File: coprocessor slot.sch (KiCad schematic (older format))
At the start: 17 parts, among them CN600 CO-PROCESSOR_SLOT, U600 74LS245, U601 74LS245, U602 74ALS245, U603 74LS245, U604 74LS245, U605 74ALS245

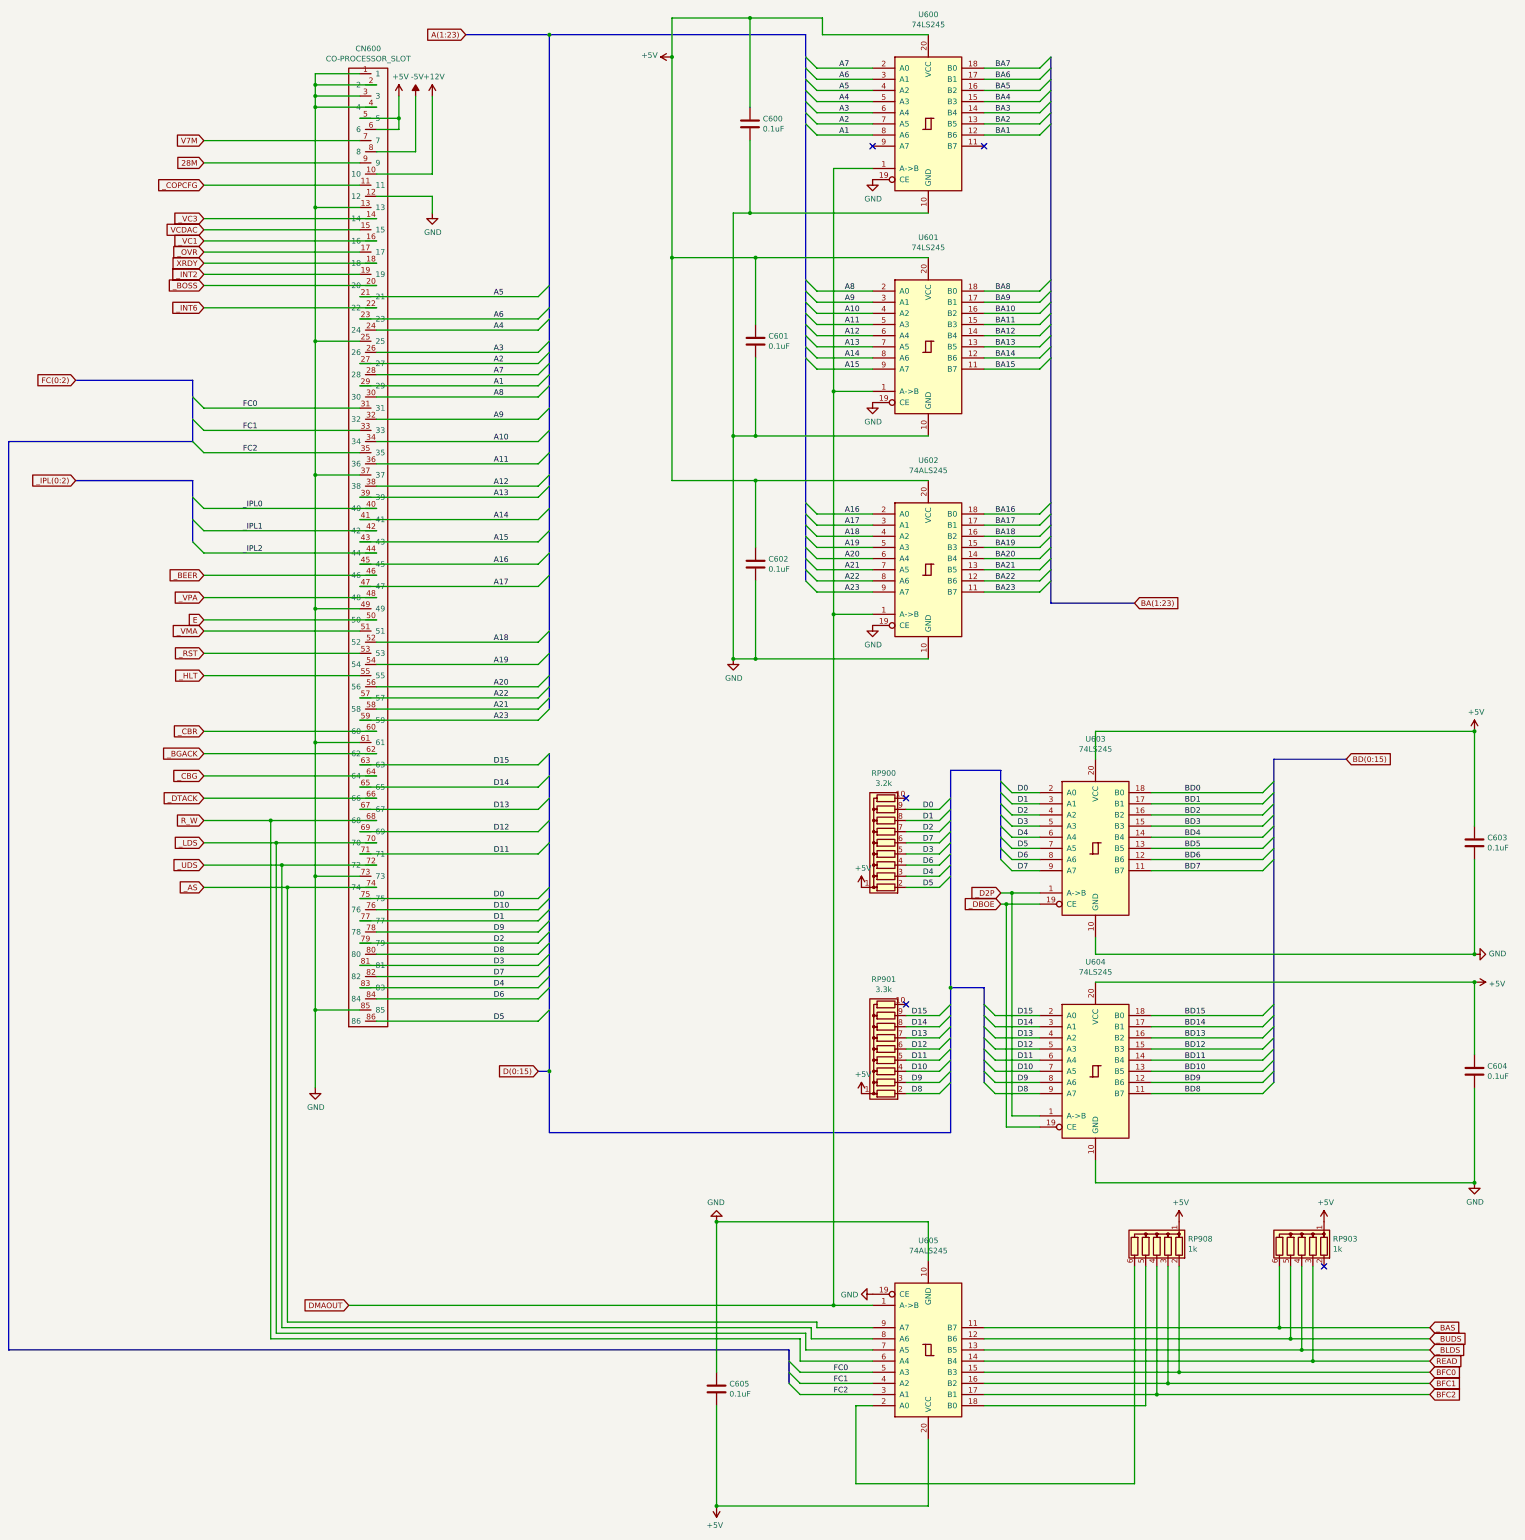
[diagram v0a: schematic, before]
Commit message: Rename bus with correct syntax
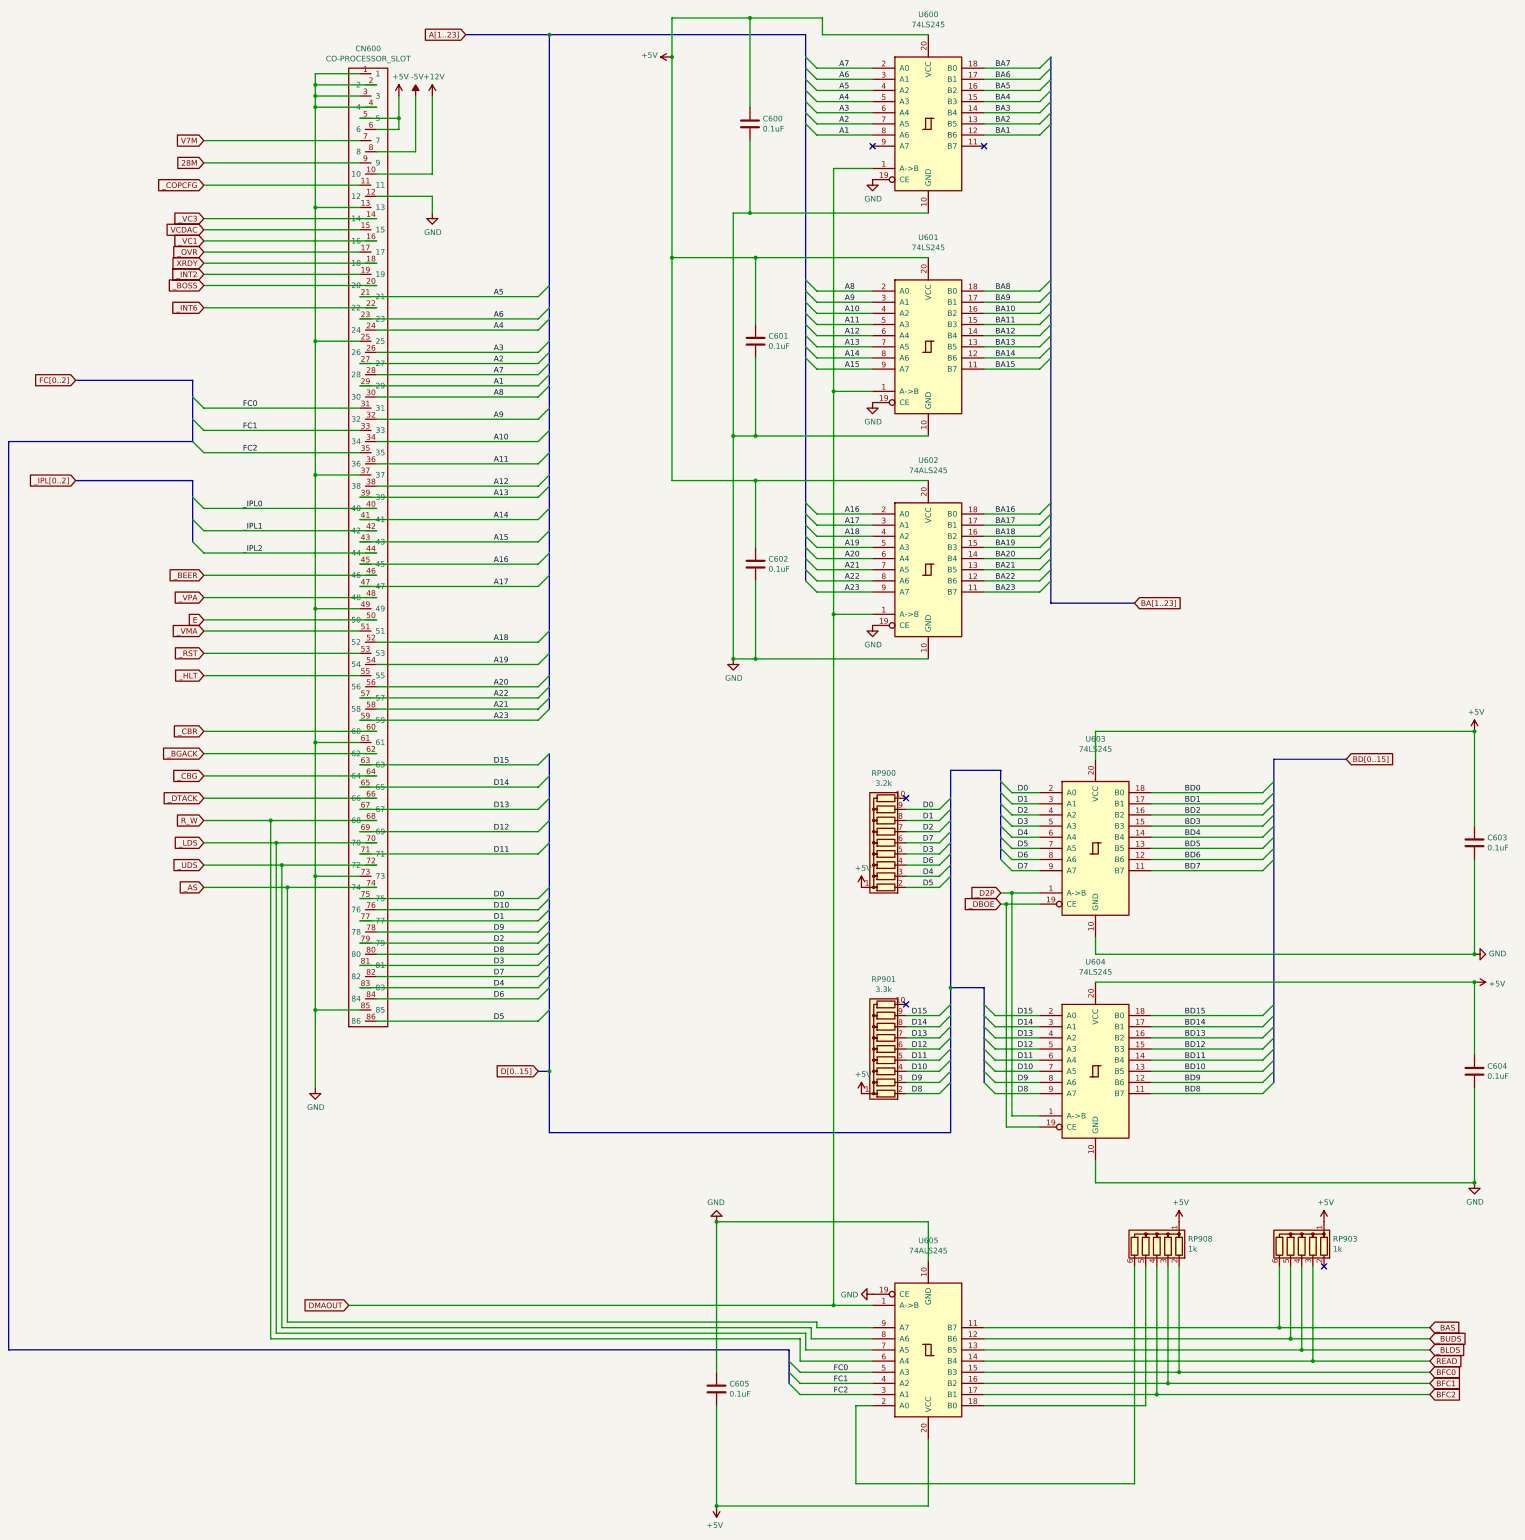
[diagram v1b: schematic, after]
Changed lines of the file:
@@
-EESchema Schematic File Version 4
+EESchema Schematic File Version 5
 LIBS:amiga2000-cache
 EELAYER 29 0
@@
 	4400 3800 3350 3800
 Text GLabel 3350 3800 0    50   Input ~ 0
-FC(0:2)
+FC[0..2]
 Wire Wire Line
 	6050 4950 4500 4950
@@
 _IPL2
 Text GLabel 3350 4700 0    50   Input ~ 0
-_IPL(0:2)
+_IPL[0..2]
 Wire Wire Line
 	6050 6950 4500 6950
@@
 	6850 700  7600 700
 Text GLabel 6850 700  0    50   Input ~ 0
-A(1:23)
+A[1..23]
 Wire Wire Line
 	5900 7250 7500 7250
@@
 	7600 10000 7500 10000
 Text GLabel 7500 10000 0    50   Input ~ 0
-D(0:15)
+D[0..15]
 $Comp
 L 74xx:74LS245 U600
@@
 	14100 7200 14750 7200
 Text GLabel 14750 7200 2    50   Input ~ 0
-BD(0:15)
+BD[0..15]
 Wire Bus Line
 	12100 5800 12850 5800
 Text GLabel 12850 5800 2    50   Input ~ 0
-BA(1:23)
+BA[1..23]
 $Comp
 L power:+5V #PWR0245
@@
 Wire Wire Line
 	11000 13900 11000 13300
-Wire Bus Line
-	4400 3800 4400 4350
-Wire Bus Line
-	4400 4700 4400 5250
-Wire Bus Line
-	9750 12500 9750 12800
-Wire Bus Line
-	11650 7300 11650 8100
-Wire Bus Line
-	11500 9250 11500 10100
-Wire Bus Line
-	11200 7300 11200 9250
-Wire Bus Line
-	11200 9250 11200 10550
-Wire Bus Line
-	7600 700  7600 6750
-Wire Bus Line
-	7600 7150 7600 10000
-Wire Bus Line
-	9900 700  9900 5600
-Wire Bus Line
-	14100 7200 14100 10100
-Wire Bus Line
-	12100 900  12100 5800
 $Comp
 L power:GND #PWR0241
@@
 $EndComp
 Connection ~ 9100 13900
+Wire Bus Line
+	4400 3800 4400 4350
+Wire Bus Line
+	4400 4700 4400 5250
+Wire Bus Line
+	9750 12500 9750 12800
+Wire Bus Line
+	11650 7300 11650 8100
+Wire Bus Line
+	11500 9250 11500 10100
+Wire Bus Line
+	11200 7300 11200 9250
+Wire Bus Line
+	11200 9250 11200 10550
+Wire Bus Line
+	7600 700  7600 6750
+Wire Bus Line
+	7600 7150 7600 10000
+Wire Bus Line
+	9900 700  9900 5600
+Wire Bus Line
+	14100 7200 14100 10100
+Wire Bus Line
+	12100 900  12100 5800
 $EndSCHEMATC

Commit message: REV 6.2 fixes applied
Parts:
- RP900: value 3.2k -> 3.3k
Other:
- note added: "REV 6.2 fixes: RP900 and RP901, 3.3k both, connected to D[0..15] were removed\nAnd instead connected directly to U603 and U604\nHere they get the same name"

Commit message: Fix the fixes
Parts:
- renumbered RP900 to RPF603, RP901 to RPF604
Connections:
- net +5V: no longer RPF603.1 (common), RPF604.1 (common)
- net D3: now also RPF603.6 (R5); no longer RPF603.5 (R4)
- net D4: now also RPF603.5 (R4); no longer RPF603.3 (R2)
- net D5: now also RPF603.4 (R3); no longer RPF603.2 (R1)
- net D6: now also RPF603.3 (R2); no longer RPF603.4 (R3)
- net D7: now also RPF603.2 (R1); no longer RPF603.6 (R5)
- net GND: now also RPF603.1 (common), RPF604.1 (common)
- net _D2P: now also RPF603.10 (R9), RPF604.10 (R9)
- no-connect marks 5 -> 3
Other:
- note added: "REV 6.2 fixes: RP900 and RP901, 3.3k both, connected to D[0..15] were removed\nAnd instead connected directly to U603 and U604"
- note removed: "REV 6.2 fixes: RP900 and RP901, 3.3k both, connected to D[0..15] were removed\nAnd instead connected directly to U603 and U604\nHere they get the same name"
- moved on the sheet: RPF603
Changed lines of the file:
@@
 $EndComp
 Connection ~ 9100 13900
+Text Notes 8450 7100 0    50   ~ 0
+REV 6.2 fixes: RP900 and RP901, 3.3k both, connected to D[0..15] were removed\nAnd instead connected directly to U603 and U604
+Entry Wire Line
+	11100 10100 11200 10000
+Entry Wire Line
+	11100 10000 11200 9900
+Entry Wire Line
+	11100 9900 11200 9800
+Entry Wire Line
+	11100 9800 11200 9700
+Entry Wire Line
+	11100 9700 11200 9600
+Entry Wire Line
+	11100 9600 11200 9500
+Entry Wire Line
+	11100 9500 11200 9400
+Text Label 10850 9400 0    50   ~ 0
+D8
+Text Label 10850 10100 0    50   ~ 0
+D15
+Text Label 10850 9900 0    50   ~ 0
+D13
+Text Label 10850 9700 0    50   ~ 0
+D11
+Text Label 10850 9500 0    50   ~ 0
+D9
+Text Label 10850 9600 0    50   ~ 0
+D10
+Text Label 10850 10000 0    50   ~ 0
+D14
+Wire Wire Line
+	10800 10000 11100 10000
+Wire Wire Line
+	10800 10100 11100 10100
+Wire Wire Line
+	10800 9800 11100 9800
+Wire Wire Line
+	10800 9600 11100 9600
+Text Label 10850 9800 0    50   ~ 0
+D12
+Wire Wire Line
+	10800 9900 11100 9900
+Wire Wire Line
+	10800 9700 11100 9700
+Wire Wire Line
+	10800 9500 11100 9500
+Entry Wire Line
+	11100 7950 11200 7850
+Wire Wire Line
+	10800 7950 11100 7950
+Text Label 10900 7550 0    50   ~ 0
+D6
+Text Label 10900 7650 0    50   ~ 0
+D5
+Entry Wire Line
+	11100 8150 11200 8050
+Wire Wire Line
+	10800 8150 11100 8150
+Entry Wire Line
+	11100 8050 11200 7950
+Entry Wire Line
+	11100 7850 11200 7750
+Entry Wire Line
+	11100 7750 11200 7650
+Entry Wire Line
+	11100 7650 11200 7550
+Entry Wire Line
+	11100 7550 11200 7450
+Wire Wire Line
+	10800 7550 11100 7550
+Text Label 10900 7950 0    50   ~ 0
+D2
+Text Label 10900 7750 0    50   ~ 0
+D4
+Text Label 10900 7850 0    50   ~ 0
+D3
+Text Label 10900 7450 0    50   ~ 0
+D7
+Text Label 10900 8150 0    50   ~ 0
+D0
+Text Label 10900 8050 0    50   ~ 0
+D1
+Wire Wire Line
+	10800 7650 11100 7650
+Wire Wire Line
+	10800 7850 11100 7850
+Wire Wire Line
+	10800 8050 11100 8050
+Wire Wire Line
+	10800 7750 11100 7750
+$Comp
+L Device:R_Network09 RPF604
+U 1 1 710DFE94
+P 10600 9800
+F 0 "RPF604" V 11225 9800 50  0000 C CNN
+F 1 "3.3k" V 11134 9800 50  0000 C CNN
+F 2 "Resistor_THT:R_Array_SIP10" V 11175 9800 50  0001 C CNN
+F 3 "http://www.vishay.com/docs/31509/csc.pdf" H 10600 9800 50  0001 C CNN
+	1    10600 9800
+	0    -1   1    0
+$EndComp
+$Comp
+L Device:R_Network09 RPF603
+U 1 1 710F61A5
+P 10600 7850
+F 0 "RPF603" V 11225 7850 50  0000 C CNN
+F 1 "3.3k" V 11134 7850 50  0000 C CNN
+F 2 "Resistor_THT:R_Array_SIP10" V 11175 7850 50  0001 C CNN
+F 3 "http://www.vishay.com/docs/31509/csc.pdf" H 10600 7850 50  0001 C CNN
+	1    10600 7850
+	0    -1   1    0
+$EndComp
+$Comp
+L power:GND #PWR0217
+U 1 1 5D5A06E2
+P 10400 7450
+F 0 "#PWR0217" H 10400 7200 50  0001 C CNN
+F 1 "GND" H 10405 7277 50  0000 C CNN
+F 2 "" H 10400 7450 50  0001 C CNN
+F 3 "" H 10400 7450 50  0001 C CNN
+	1    10400 7450
+	-1   0    0    1
+$EndComp
+$Comp
+L power:GND #PWR0218
+U 1 1 5D5A112B
+P 10400 9400
+F 0 "#PWR0218" H 10400 9150 50  0001 C CNN
+F 1 "GND" H 10405 9227 50  0000 C CNN
+F 2 "" H 10400 9400 50  0001 C CNN
+F 3 "" H 10400 9400 50  0001 C CNN
+	1    10400 9400
+	-1   0    0    1
+$EndComp
+Entry Wire Line
+	11100 7450 11200 7350
+Entry Wire Line
+	11100 9400 11200 9300
+Wire Wire Line
+	11100 9400 10800 9400
+Wire Wire Line
+	10800 10200 11300 10200
+Wire Wire Line
+	11300 10200 11300 10400
+Wire Wire Line
+	11300 10400 11750 10400
+Connection ~ 11750 10400
+Wire Wire Line
+	10800 7450 11100 7450
+Wire Wire Line
+	10800 8250 11750 8250
+Wire Wire Line
+	11750 8250 11750 8400
 Wire Bus Line
 	4400 3800 4400 4350
@@
 Wire Bus Line
 	12100 900  12100 5800
-Text Notes 8450 7100 0    50   ~ 0
-REV 6.2 fixes: RP900 and RP901, 3.3k both, connected to D[0..15] were removed\nAnd instead connected directly to U603 and U604\nHere they get the same name
-Entry Wire Line
-	11100 10200 11200 10100
-Entry Wire Line
-	11100 10100 11200 10000
-Entry Wire Line
-	11100 10000 11200 9900
-Entry Wire Line
-	11100 9900 11200 9800
-Entry Wire Line
-	11100 9800 11200 9700
-Entry Wire Line
-	11100 9700 11200 9600
-Entry Wire Line
-	11100 9600 11200 9500
-Entry Wire Line
-	11100 9500 11200 9400
-Text Label 10850 10200 0    50   ~ 0
-D8
-Text Label 10850 9500 0    50   ~ 0
-D15
-Text Label 10850 9700 0    50   ~ 0
-D13
-Text Label 10850 9900 0    50   ~ 0
-D11
-Text Label 10850 10100 0    50   ~ 0
-D9
-Text Label 10850 10000 0    50   ~ 0
-D10
-Text Label 10850 9600 0    50   ~ 0
-D14
-Wire Wire Line
-	10800 10000 11100 10000
-Wire Wire Line
-	10800 10200 11100 10200
-Wire Wire Line
-	10800 10100 11100 10100
-Wire Wire Line
-	10800 9800 11100 9800
-Wire Wire Line
-	10800 9600 11100 9600
-Text Label 10850 9800 0    50   ~ 0
-D12
-Wire Wire Line
-	10800 9900 11100 9900
-Wire Wire Line
-	10800 9700 11100 9700
-Wire Wire Line
-	10800 9500 11100 9500
-NoConn ~ 10800 9400
-Entry Wire Line
-	11100 8150 11200 8050
-Wire Wire Line
-	10800 8150 11100 8150
-Text Label 10950 8150 0    50   ~ 0
-D6
-Text Label 10950 8350 0    50   ~ 0
-D5
-Entry Wire Line
-	11100 8350 11200 8250
-Wire Wire Line
-	10800 8350 11100 8350
-Entry Wire Line
-	11100 8250 11200 8150
-Entry Wire Line
-	11100 8050 11200 7950
-Entry Wire Line
-	11100 7950 11200 7850
-Entry Wire Line
-	11100 7850 11200 7750
-Entry Wire Line
-	11100 7750 11200 7650
-Entry Wire Line
-	11100 7650 11200 7550
-Wire Wire Line
-	10800 7750 11100 7750
-Text Label 10950 7850 0    50   ~ 0
-D2
-Text Label 10950 8250 0    50   ~ 0
-D4
-Text Label 10950 8050 0    50   ~ 0
-D3
-Text Label 10950 7950 0    50   ~ 0
-D7
-Text Label 10950 7650 0    50   ~ 0
-D0
-Text Label 10950 7750 0    50   ~ 0
-D1
-Wire Wire Line
-	10800 7850 11100 7850
-Wire Wire Line
-	10800 8050 11100 8050
-Wire Wire Line
-	10800 8250 11100 8250
-Wire Wire Line
-	10800 7950 11100 7950
-Wire Wire Line
-	10800 7650 11100 7650
-NoConn ~ 10800 7550
-$Comp
-L power:+5V #PWR0245
-U 1 1 71228FE0
-P 10400 10200
-F 0 "#PWR0245" H 10400 10050 50  0001 C CNN
-F 1 "+5V" H 10415 10373 50  0000 C CNN
-F 2 "" H 10400 10200 50  0001 C CNN
-F 3 "" H 10400 10200 50  0001 C CNN
-	1    10400 10200
-	1    0    0    -1
-$EndComp
-$Comp
-L power:+5V #PWR0244
-U 1 1 71229744
-P 10400 8350
-F 0 "#PWR0244" H 10400 8200 50  0001 C CNN
-F 1 "+5V" H 10415 8523 50  0000 C CNN
-F 2 "" H 10400 8350 50  0001 C CNN
-F 3 "" H 10400 8350 50  0001 C CNN
-	1    10400 8350
-	1    0    0    -1
-$EndComp
-$Comp
-L Device:R_Network09 RP901
-U 1 1 710DFE94
-P 10600 9800
-F 0 "RP901" V 11225 9800 50  0000 C CNN
-F 1 "3.3k" V 11134 9800 50  0000 C CNN
-F 2 "Resistor_THT:R_Array_SIP10" V 11175 9800 50  0001 C CNN
-F 3 "http://www.vishay.com/docs/31509/csc.pdf" H 10600 9800 50  0001 C CNN
-	1    10600 9800
-	0    -1   -1   0
-$EndComp
-$Comp
-L Device:R_Network09 RP900
-U 1 1 710F61A5
-P 10600 7950
-F 0 "RP900" V 11225 7950 50  0000 C CNN
-F 1 "3.3k" V 11134 7950 50  0000 C CNN
-F 2 "Resistor_THT:R_Array_SIP10" V 11175 7950 50  0001 C CNN
-F 3 "http://www.vishay.com/docs/31509/csc.pdf" H 10600 7950 50  0001 C CNN
-	1    10600 7950
-	0    -1   -1   0
-$EndComp
 $EndSCHEMATC

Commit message: Associate footprints with components
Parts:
- U600, U601, U602, U603, U604, U605: footprint (none) -> Package_DIP:DIP-20_W7.62mm_Socket
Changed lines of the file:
@@
 F 0 "U600" H 11000 2481 50  0000 C CNN
 F 1 "74LS245" H 11000 2390 50  0000 C CNN
-F 2 "" H 11000 1500 50  0001 C CNN
+F 2 "Package_DIP:DIP-20_W7.62mm_Socket" H 11000 1500 50  0001 C CNN
 F 3 "http://www.ti.com/lit/gpn/sn74LS245" H 11000 1500 50  0001 C CNN
 	1    11000 1500
@@
 F 0 "U601" H 11000 4481 50  0000 C CNN
 F 1 "74LS245" H 11000 4390 50  0000 C CNN
-F 2 "" H 11000 3500 50  0001 C CNN
+F 2 "Package_DIP:DIP-20_W7.62mm_Socket" H 11000 3500 50  0001 C CNN
 F 3 "http://www.ti.com/lit/gpn/sn74LS245" H 11000 3500 50  0001 C CNN
 	1    11000 3500
@@
 F 0 "U602" H 11000 6481 50  0000 C CNN
 F 1 "74ALS245" H 11000 6390 50  0000 C CNN
-F 2 "" H 11000 5500 50  0001 C CNN
+F 2 "Package_DIP:DIP-20_W7.62mm_Socket" H 11000 5500 50  0001 C CNN
 F 3 "http://www.ti.com/lit/gpn/sn74LS245" H 11000 5500 50  0001 C CNN
 	1    11000 5500
@@
 F 0 "U603" H 12500 8981 50  0000 C CNN
 F 1 "74LS245" H 12500 8890 50  0000 C CNN
-F 2 "" H 12500 8000 50  0001 C CNN
+F 2 "Package_DIP:DIP-20_W7.62mm_Socket" H 12500 8000 50  0001 C CNN
 F 3 "http://www.ti.com/lit/gpn/sn74LS245" H 12500 8000 50  0001 C CNN
 	1    12500 8000
@@
 F 0 "U604" H 12500 10981 50  0000 C CNN
 F 1 "74LS245" H 12500 10890 50  0000 C CNN
-F 2 "" H 12500 10000 50  0001 C CNN
+F 2 "Package_DIP:DIP-20_W7.62mm_Socket" H 12500 10000 50  0001 C CNN
 F 3 "http://www.ti.com/lit/gpn/sn74LS245" H 12500 10000 50  0001 C CNN
 	1    12500 10000
@@
 F 0 "U605" H 11000 11519 50  0000 C CNN
 F 1 "74ALS245" H 11000 11610 50  0000 C CNN
-F 2 "" H 11000 12500 50  0001 C CNN
+F 2 "Package_DIP:DIP-20_W7.62mm_Socket" H 11000 12500 50  0001 C CNN
 F 3 "http://www.ti.com/lit/gpn/sn74LS245" H 11000 12500 50  0001 C CNN
 	1    11000 12500
